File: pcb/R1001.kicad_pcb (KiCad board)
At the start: 4 copper layers, 45 x 33.3 mm, 32 parts, among them J1 PCIEXPRESS-X1, J2 CONN_01X04, U1 DRV8825, U2 74LS157, U3 EFM8BB10F2G

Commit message: updated design, placed driver
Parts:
- removed MP1: HEATSINK_V7700W, Main:HEATSINK_V7700W
- C10, C5, C7, J2, U1: moved to B.Cu
- C12, R3: moved to F.Cu
- moved R16 33.5 mm to (125.2, 63.7)
- moved C3 29.5 mm to (191.2, 96.4)
- moved R17 27.7 mm to (132.1, 63.9)
- moved R6 25.9 mm to (180.1, 99.8)
- moved R11 21.8 mm to (172.9, 100.2)
- moved R7 18.7 mm to (144.8, 64.9)
- moved R5 11.0 mm to (162.0, 86.0), turned to 270 degrees
- moved R4 10.6 mm to (138.2, 62.9)
- moved C14 9.56 mm to (148.8, 63.7)
- moved C5 8.22 mm to (157.6, 78.7), turned to 90 degrees
- moved C10 7.51 mm to (155.6, 76.2), turned to 180 degrees
- moved C9 6.25 mm to (158.4, 66.0)
- moved R2 6.11 mm to (154.4, 66.1)
- moved U1 5.70 mm to (152.0, 82.0)
- moved R3 5.52 mm to (157.6, 79.3), turned to 90 degrees
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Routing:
- net +3V3: track 104.5 -> 10.8 mm, vias 3 -> 0
- net HT: track 45.8 -> 111.5 mm, vias 17 -> 2
- net /~D1_FAULT: track 51.0 -> 0.00 mm, vias 2 -> 0
- net PX3_STEP: track 51.2 -> 2.30 mm, vias 2 -> 0
- net ID0: track 50.2 -> 2.30 mm, vias 3 -> 0
- net GND: track 66.2 -> 20.3 mm, vias 19 -> 0
- net PX2_~ENBL: track 47.7 -> 2.30 mm, vias 4 -> 0
- net PX1_DIR: track 47.7 -> 2.30 mm, vias 3 -> 0
- net ID1: track 47.4 -> 3.60 mm, vias 3 -> 0
- net ID2: track 47.0 -> 4.62 mm, vias 3 -> 0
- net ID3: track 41.2 -> 2.34 mm, vias 3 -> 0
- net C2D: track 40.3 -> 2.30 mm, vias 2 -> 0
- net /STEP: track 32.0 -> 0.00 mm, vias 2 -> 0
- net /MCU_DECAY: track 30.3 -> 0.00 mm
- net /MCU_PWMVREF: track 29.4 -> 0.00 mm, vias 2 -> 0
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- removed copper zone on F.Cu, net HT

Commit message: completed layout
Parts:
- removed C2: 0.1uF, Capacitors_SMD:C_0603
- C1, U3: moved to B.Cu
- C3: footprint Capacitors_SMD:c_elec_6.3x5.3 -> Capacitors_SMD:c_elec_8x6.5
- C9, R2: moved to F.Cu
- moved C3 59.8 mm to (131.9, 88.5)
- moved R6 42.4 mm to (142.9, 79.5), turned to 270 degrees
- moved R11 33.8 mm to (146.3, 79.4), turned to 270 degrees
- moved C14 24.8 mm to (148.0, 88.5), turned to 270 degrees
- moved R16 22.1 mm to (141.2, 78.9), turned to 270 degrees
- moved C9 21.7 mm to (156.5, 87.6), turned to 270 degrees
- moved R2 21.6 mm to (154.8, 87.7), turned to 270 degrees
- moved R17 15.9 mm to (139.5, 78.0), turned to 270 degrees
- moved R1 11.5 mm to (144.6, 80.1)
- moved R14 11.2 mm to (139.8, 88.2), turned to 0 degrees
- moved R7 10.0 mm to (147.7, 74.5), turned to 270 degrees
- moved R13 9.80 mm to (139.8, 86.5), turned to 0 degrees
- moved R12 8.91 mm to (139.8, 84.8), turned to 0 degrees
- moved R4 8.85 mm to (141.0, 71.3)
- moved R10 8.65 mm to (139.8, 83.1), turned to 0 degrees
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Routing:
- net PX2_~ENBL: track 2.30 -> 53.0 mm, vias 0 -> 3
- net +3V3: track 10.8 -> 60.4 mm, vias 0 -> 7
- net PX1_DIR: track 2.30 -> 48.0 mm, vias 0 -> 4
- net PX3_STEP: track 2.30 -> 47.5 mm, vias 0 -> 3
- net HT: track 111.5 -> 149.8 mm, vias 2 -> 10
- net ~MRESET: track 2.30 -> 32.6 mm, vias 0 -> 2
- net SCL: track 2.30 -> 30.7 mm, vias 0 -> 2
- net /~ENBL: track 0.00 -> 26.6 mm, vias 0 -> 2
- net /STEP: track 0.00 -> 26.0 mm, vias 0 -> 3
- net SDA: track 2.30 -> 28.0 mm, vias 0 -> 2
- net C2D: track 2.30 -> 26.5 mm, vias 0 -> 2
- net ID0: track 2.30 -> 25.1 mm, vias 0 -> 2
- net /SLAVE_ENABLE: track 0.00 -> 21.8 mm, vias 0 -> 2
- net ID3: track 2.34 -> 22.5 mm, vias 0 -> 2
- net ID1: track 3.60 -> 22.4 mm, vias 0 -> 2
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- added copper zone on In1.Cu, net +3V3
- removed copper zone on In1.Cu, net GND
- removed copper zone on In1.Cu, net HT

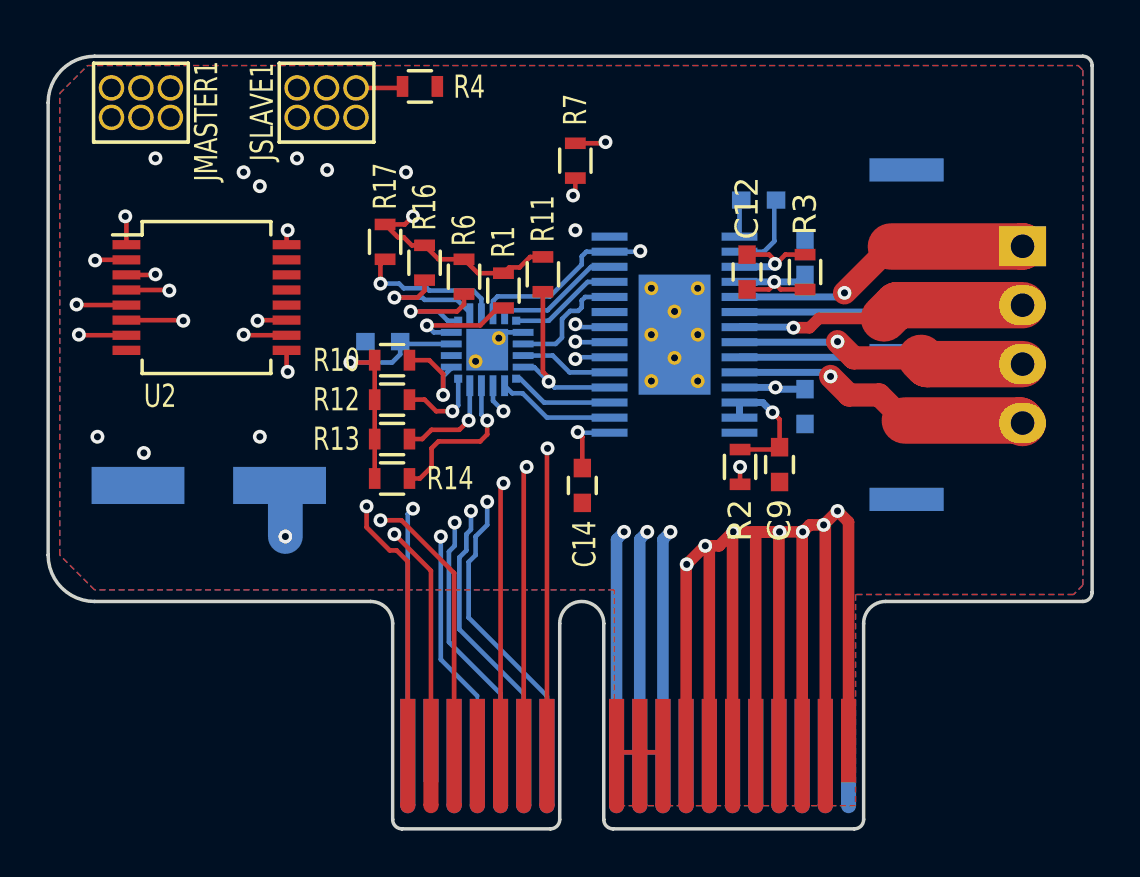
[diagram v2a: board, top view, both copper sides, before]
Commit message: created solder mask opening for large heat sink on bottom layer
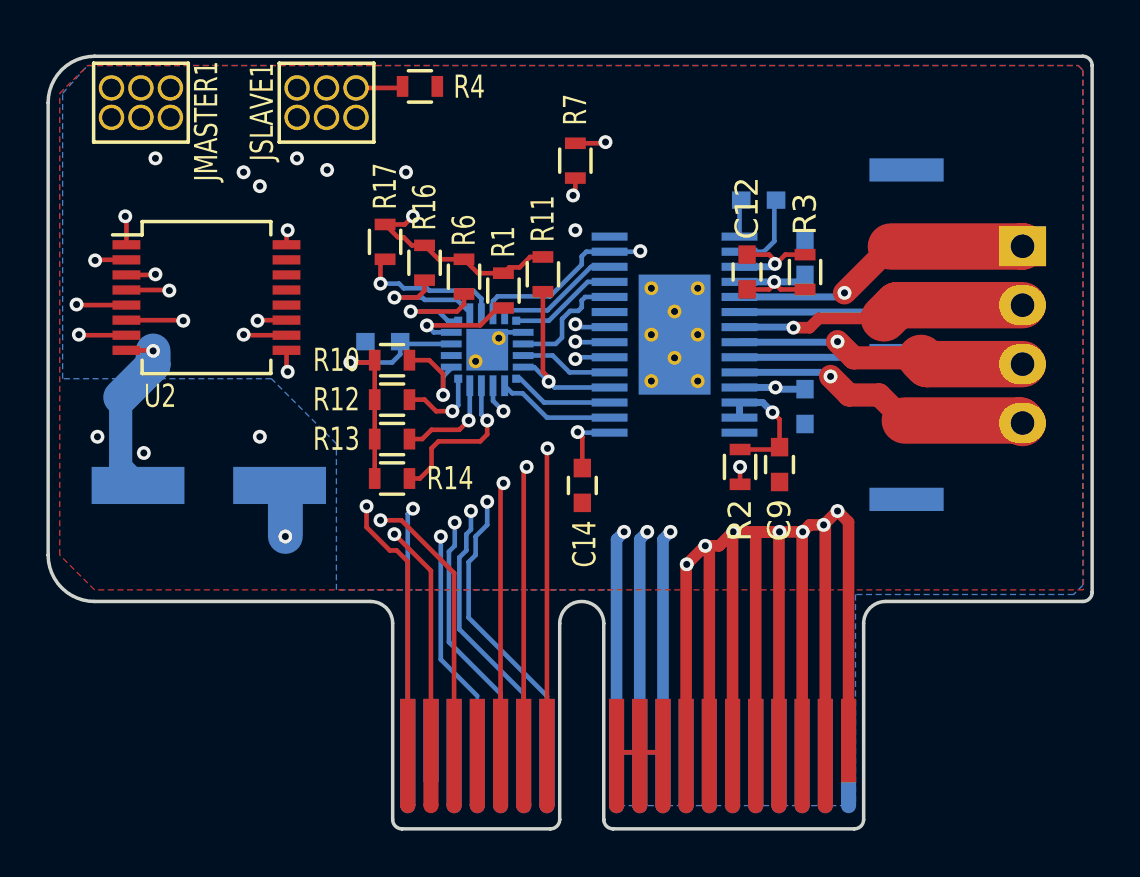
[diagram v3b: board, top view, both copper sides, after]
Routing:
- net GND: track 20.3 -> 28.1 mm, vias 0 -> 1
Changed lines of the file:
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@@
     (thickness 1.6)
     (drawings 22)
-    (tracks 541)
+    (tracks 549)
     (zones 0)
     (modules 30)
@@
   (layers
     (0 F.Cu power)
-    (1 In1.Cu signal)
-    (2 In2.Cu signal)
-    (31 B.Cu power)
+    (1 In1.Cu signal hide)
+    (2 In2.Cu signal hide)
+    (31 B.Cu power hide)
     (32 B.Adhes user)
     (33 F.Adhes user)
@@
     (36 B.SilkS user)
     (37 F.SilkS user)
-    (38 B.Mask user)
-    (39 F.Mask user)
+    (38 B.Mask user hide)
+    (39 F.Mask user hide)
     (40 Dwgs.User user)
     (41 Cmts.User user)
@@
   (gr_line (start 148.95 94.45) (end 148.95 102.9) (angle 90) (layer Edge.Cuts) (width 0.15))
   (gr_line (start 147.05 94.45) (end 147.05 102.9) (angle 90) (layer Edge.Cuts) (width 0.15))
+  (segment (start 128.87446 88.5) (end 128.87446 88.44946) (width 1) (layer B.Cu) (net 1))
+  (segment (start 128.87446 88.44946) (end 128.125 87.7) (width 1) (layer B.Cu) (net 1))
+  (segment (start 128.125 87.7) (end 128.125 84.7) (width 1) (layer B.Cu) (net 1))
+  (segment (start 128.125 84.7) (end 129.525 83.3) (width 1.5) (layer B.Cu) (net 1))
+  (segment (start 129.525 83.3) (end 129.525 82.7) (width 1.5) (layer B.Cu) (net 1))
+  (segment (start 128.375 82.675) (end 129.5 82.675) (width 0.2) (layer F.Cu) (net 1))
+  (via (at 129.525 82.7) (size 0.6) (drill 0.3) (layers F.Cu B.Cu) (net 1))
+  (segment (start 129.5 82.675) (end 129.525 82.7) (width 0.2) (layer F.Cu) (net 1))
   (segment (start 145.475 81.9) (end 144.675 81.9) (width 0.2) (layer B.Cu) (net 1))
   (segment (start 144.675 81.9) (end 143.925 82.65) (width 0.2) (layer B.Cu) (net 1))
@@
       (pts
         (xy 169.6 70.6) (xy 169.6 92.8) (xy 169.2 93.2) (xy 159.8 93.2) (xy 159.8 102.3)
-        (xy 149.4 102.3) (xy 149.4 93) (xy 127 93) (xy 125.5 91.5) (xy 125.5 71.6)
-        (xy 126.7 70.4) (xy 169.4 70.4) (xy 169.6 70.6)
+        (xy 149.4 102.3) (xy 149.4 93) (xy 137.425 93) (xy 137.425 86.7) (xy 134.625 83.9)
+        (xy 125.625 83.9) (xy 125.625 71.6) (xy 126.7 70.4) (xy 169.4 70.4) (xy 169.6 70.6)
       )
     )
@@
     (polygon
       (pts
-        (xy 169.6 70.6) (xy 169.6 92.8) (xy 169.2 93.2) (xy 159.8 93.2) (xy 159.8 102.3)
-        (xy 149.4 102.3) (xy 149.4 93) (xy 127 93) (xy 125.5 91.5) (xy 125.5 71.6)
+        (xy 169.6 70.6) (xy 169.625 93) (xy 127 93) (xy 125.5 91.5) (xy 125.5 71.6)
         (xy 126.7 70.4) (xy 169.4 70.4) (xy 169.6 70.6)
       )
     )
+  )
+  (zone (net 0) (net_name "") (layer B.Mask) (hatch edge 0.508)
+    (connect_pads (clearance 0.22))
+    (min_thickness 0.254)
+    (fill yes (arc_segments 16) (thermal_gap 0.508) (thermal_bridge_width 0.508))
+    (polygon
+      (pts
+        (xy 155.125 70.9) (xy 155.125 73) (xy 159.125 73) (xy 159.125 70.9) (xy 159.025 70.9)
+      )
+    )

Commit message: optimized layout for thermal
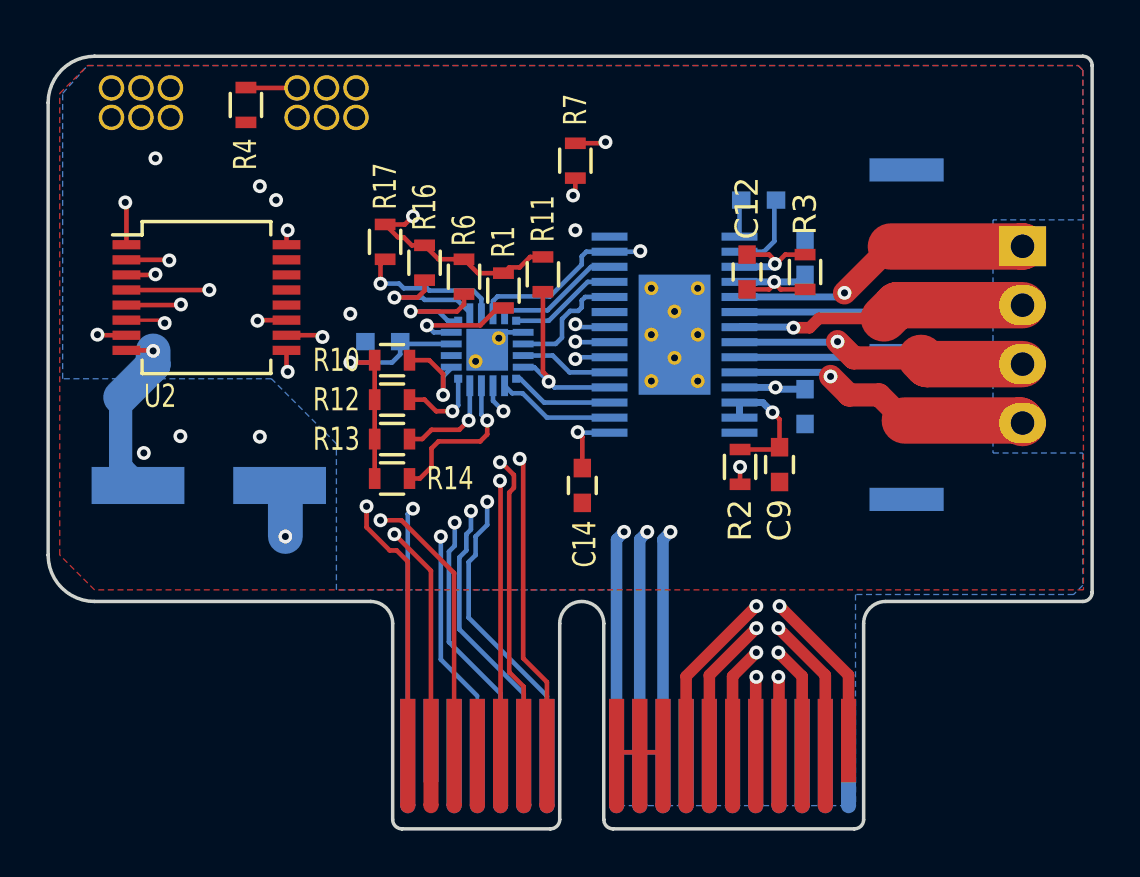
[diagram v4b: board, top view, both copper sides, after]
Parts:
- JMASTER1, JSLAVE1: moved to B.Cu
- moved R4 7.54 mm to (133.5, 72.1), turned to 270 degrees
- turned JMASTER1 to 180 degrees
- turned JSLAVE1 to 180 degrees
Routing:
- net HT: track 149.8 -> 117.6 mm, vias 10 -> 11
- net /SLAVE_ENABLE: track 21.8 -> 15.9 mm
- net /S_~ENBL: track 16.4 -> 22.2 mm, vias 1 -> 2
- net +3V3: track 60.4 -> 66.0 mm
- net PX2_~ENBL: track 53.0 -> 48.5 mm
- net /S_DIR: track 14.8 -> 11.2 mm, vias 3 -> 1
- net /S_STEP: track 14.1 -> 16.5 mm, vias 3 -> 2
- net /~ENBL: track 26.6 -> 24.3 mm
- net /STEP: track 26.0 -> 26.8 mm
- net PX1_DIR: track 48.0 -> 47.3 mm

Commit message: v1.0.0-beta complete
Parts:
- added G***: LOGO, pluggee:pluggee-QRNEG-085X085, F.Cu at (161.8, 89.2)
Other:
- board text added: "R1001A v1.0.0-beta DRV8825 Stepper Motor Driver http://plugg.ee"
- board text added: "plugg.ee Labs 2016"

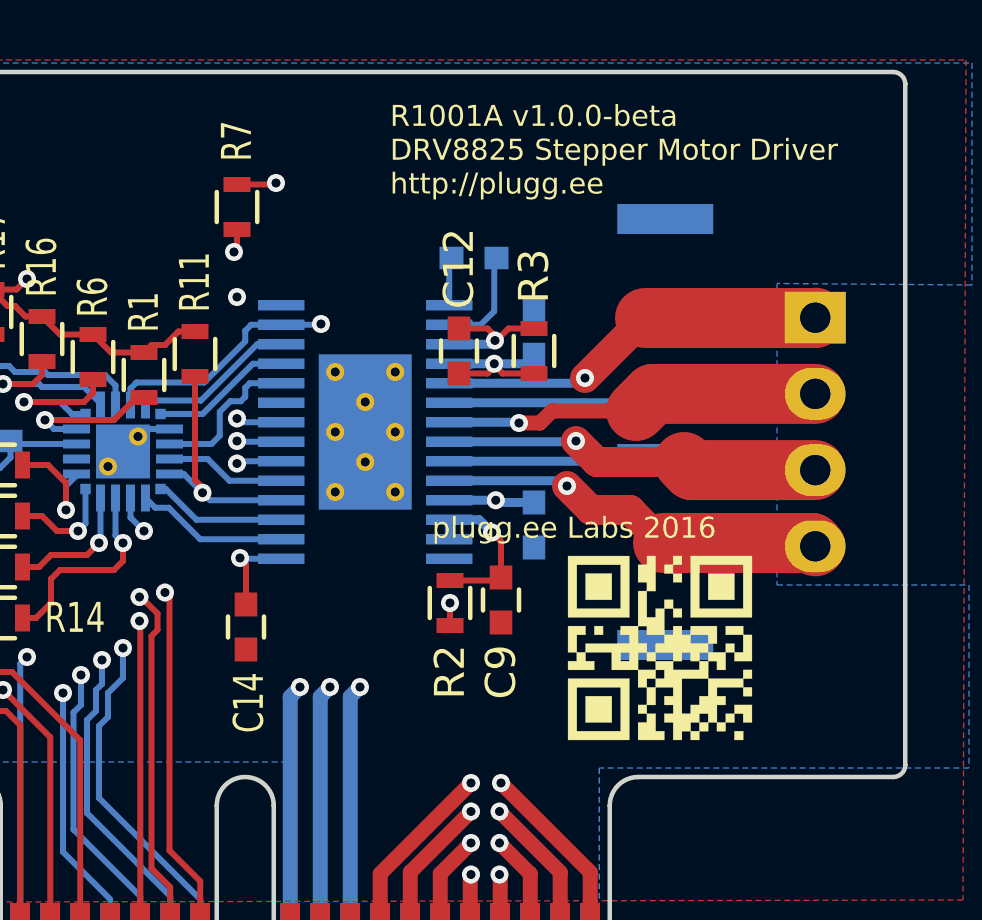
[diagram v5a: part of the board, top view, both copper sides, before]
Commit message: added silk screen to motor pins
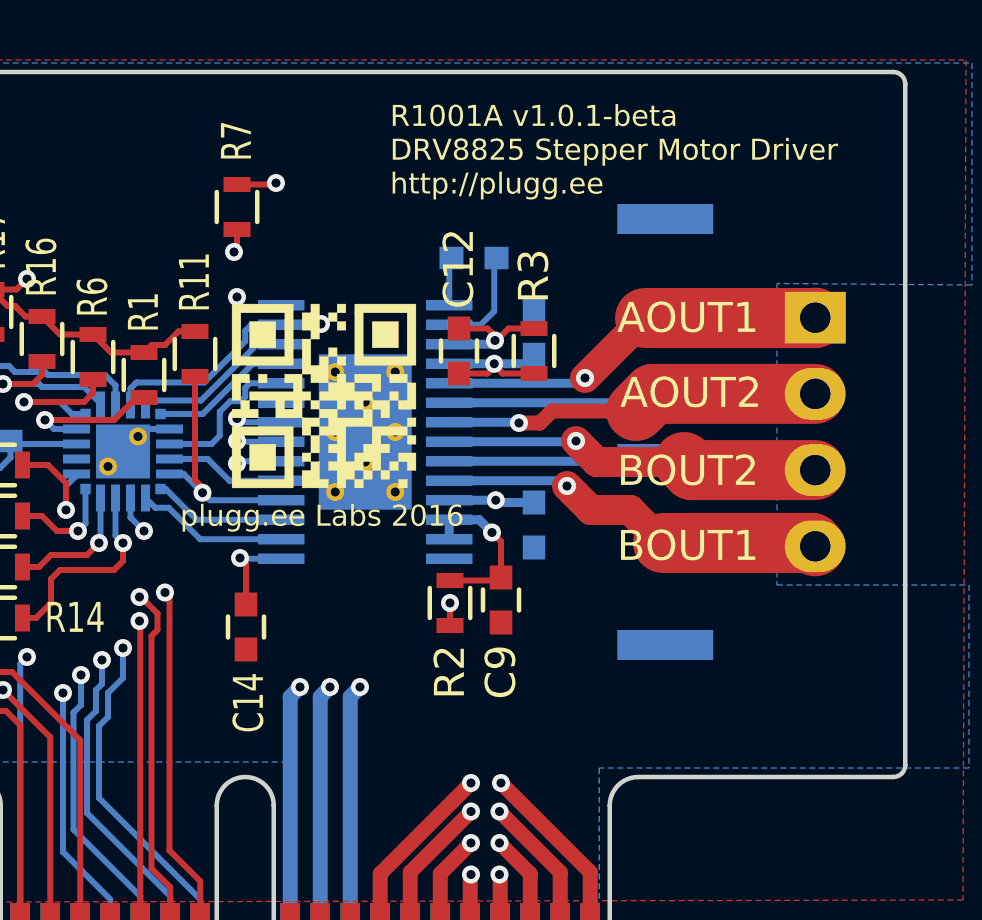
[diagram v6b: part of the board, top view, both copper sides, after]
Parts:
- moved G*** 14.0 mm to (150.6, 80.8)
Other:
- board text added: "AOUT1"
- board text added: "AOUT2"
- board text added: "BOUT1"
- board text added: "BOUT2"
- board text added: "R1001A v1.0.1-beta DRV8825 Stepper Motor Driver http://plugg.ee"
- board text removed: "R1001A v1.0.0-beta DRV8825 Stepper Motor Driver http://plugg.ee"
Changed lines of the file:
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@@
     (area 123.225 67.573799 172.225001 103.524461)
     (thickness 1.6)
-    (drawings 24)
+    (drawings 28)
     (tracks 565)
     (zones 0)
@@
   (page A4)
   (layers
-    (0 F.Cu power hide)
+    (0 F.Cu power)
     (1 In1.Cu signal hide)
     (2 In2.Cu signal hide)
-    (31 B.Cu power hide)
+    (31 B.Cu power)
     (32 B.Adhes user)
     (33 F.Adhes user)
@@
     (user_trace_width 2)
     (trace_clearance 0.15)
-    (zone_clearance 0.22)
+    (zone_clearance 0.508)
     (zone_45_only yes)
     (trace_min 0.15)
@@
   )
   (module pluggee:pluggee-QRNEG-085X085 (layer F.Cu)
-    (at 161.825 89.2)
+    (at 150.625 80.8)
     (fp_text reference G*** (at 0 0) (layer F.SilkS) hide
       (effects (font (thickness 0.3)))
@@
       (xy 2.481609 -1.605747)) (layer F.SilkS) (width 0.01))
   )
-  (gr_text "plugg.ee Labs 2016" (at 154.225 85.2) (layer F.SilkS)
+  (gr_text BOUT1 (at 165.125 85.8) (layer F.SilkS)
+    (effects (font (size 1 1) (thickness 0.2)) (justify right))
+  )
+  (gr_text BOUT2 (at 165.125 83.3) (layer F.SilkS)
+    (effects (font (size 1 1) (thickness 0.2)) (justify right))
+  )
+  (gr_text AOUT2 (at 165.225 80.7) (layer F.SilkS)
+    (effects (font (size 1 1) (thickness 0.2)) (justify right))
+  )
+  (gr_text AOUT1 (at 165.125 78.2) (layer F.SilkS)
+    (effects (font (size 1 1) (thickness 0.2)) (justify right))
+  )
+  (gr_text "plugg.ee Labs 2016" (at 145.825 84.8) (layer F.SilkS)
     (effects (font (size 0.7 0.7) (thickness 0.15)) (justify left))
   )
-  (gr_text "R1001A v1.0.0-beta\nDRV8825 Stepper Motor Driver\nhttp://plugg.ee" (at 152.825 72.6) (layer F.SilkS)
+  (gr_text "R1001A v1.0.1-beta\nDRV8825 Stepper Motor Driver\nhttp://plugg.ee" (at 152.825 72.6) (layer F.SilkS)
     (effects (font (size 0.7 0.7) (thickness 0.15)) (justify left))
   )
